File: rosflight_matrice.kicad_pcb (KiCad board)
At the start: 2 copper layers, 80 x 49 mm, 21 parts, among them J1 Left, J10 I2C, J11 I2C, J2 Right, J3 Power, J4 Servo 1-3, J5 Servo 4-6, J6 Main, J7 Flexi-IO, J8 Flexi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

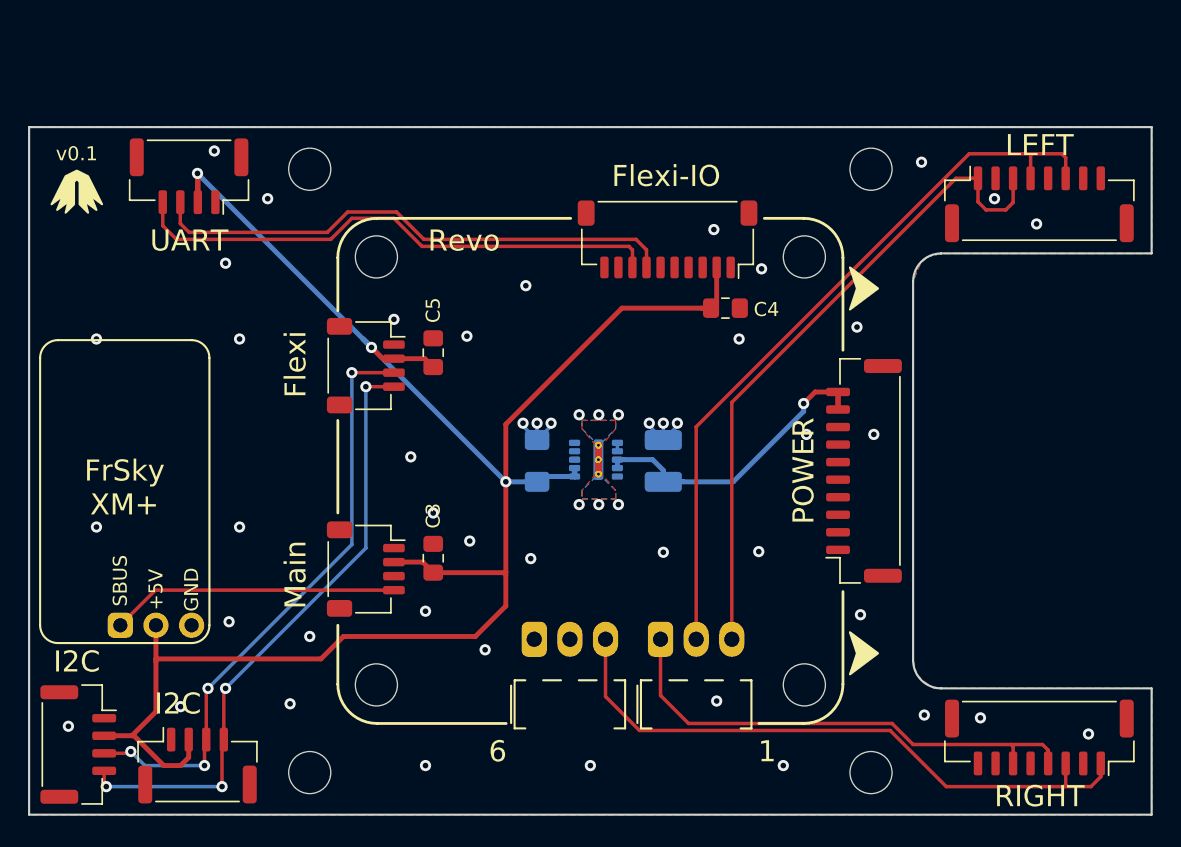
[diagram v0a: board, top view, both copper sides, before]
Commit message: New switching voltage regulator and updated layout
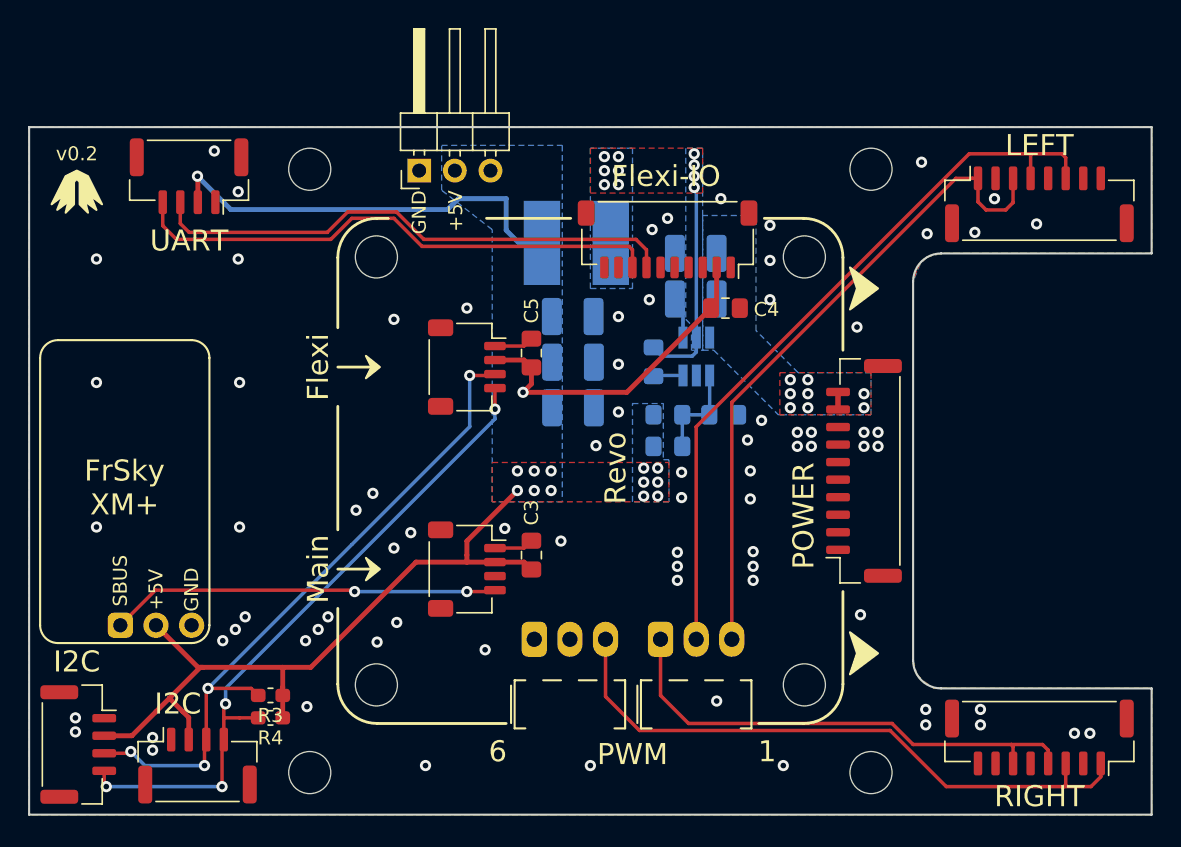
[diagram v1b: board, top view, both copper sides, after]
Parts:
- added C10: 22uF, Capacitor_SMD:C_1210_3225Metric_Pad1.42x2.65mm_HandSolder, B.Cu at (148.8, 95.5)
- added C6: 100nF, Capacitor_SMD:C_0805_2012Metric_Pad1.15x1.40mm_HandSolder, B.Cu at (154.5, 92.2)
- added C7: 100pF, Capacitor_SMD:C_0805_2012Metric_Pad1.15x1.40mm_HandSolder, B.Cu at (155.5, 98.2)
- added C8: 22uF, Capacitor_SMD:C_1210_3225Metric_Pad1.42x2.65mm_HandSolder, B.Cu at (148.7, 89.0)
- added C9: 22uF, Capacitor_SMD:C_1210_3225Metric_Pad1.42x2.65mm_HandSolder, B.Cu at (148.8, 92.2)
- added J12: 5V, Connector_PinHeader_2.54mm:PinHeader_1x03_P2.54mm_Horizontal, F.Cu at (137.8, 78.6)
- added L1: 6.8uH, quadrotor:SRN6045_HandSolder, B.Cu at (149.0, 83.8)
- added R1: 100k, Resistor_SMD:R_0805_2012Metric_Pad1.15x1.40mm_HandSolder, B.Cu at (155.5, 96.0)
- added R2: 13.7k, Resistor_SMD:R_0805_2012Metric_Pad1.15x1.40mm_HandSolder, B.Cu at (159.5, 96.0)
- added R3: 4.7k, Resistor_SMD:R_0603_1608Metric_Pad1.05x0.95mm_HandSolder, F.Cu at (127.2, 116.0)
- added R4: 4.7k, Resistor_SMD:R_0603_1608Metric_Pad1.05x0.95mm_HandSolder, F.Cu at (127.2, 117.6)
- C2: value 22uF -> 10uF; footprint Capacitor_SMD:C_1206_3216Metric_Pad1.42x1.75mm_HandSolder -> Capacitor_SMD:C_1210_3225Metric_Pad1.42x2.65mm_HandSolder
- U1: value LMZM23600V5SIL -> TPS54202; footprint Package_LGA:Texas_SIL0010A_MicroSiP-10-1EP_3.8x3mm_P0.6mm_EP0.7x2.9mm_ThermalVias -> Package_TO_SOT_SMD:SOT-23-6_Handsoldering
- moved C2 16.2 mm to (157.5, 87.8), turned to 180 degrees
- moved C1 15.0 mm to (157.5, 84.5), turned to 180 degrees
- moved U1 10.3 mm to (157.6, 91.8), turned to 270 degrees
- moved J8 7.20 mm to (141.2, 92.6)
- moved J6 7.20 mm to (141.2, 107.0)
- moved C3 7.00 mm to (145.8, 106.0)
- moved C5 7.00 mm to (145.8, 91.6)
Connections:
- C2 pad 1: +5V -> +BATT
- U1 pad 2: GND -> Net-(C6-Pad1)
- U1 pad 4: +BATT -> Net-(C7-Pad2)
- U1 pad 6: +5V -> Net-(C6-Pad2)
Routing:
- net +5V: track 129.6 -> 108.2 mm, vias 3 -> 14
- net +BATT: track 21.7 -> 1.25 mm, vias 1 -> 8
- net Net-(C6-Pad1): track 0.00 -> 15.2 mm, vias 0 -> 10
- net /SBUS: track 20.5 -> 27.8 mm, vias 0 -> 2
- net Net-(C7-Pad2): track 0.00 -> 6.99 mm
- net /SCL: track 43.0 -> 48.9 mm
- net /SDA: track 44.2 -> 48.3 mm
- net Net-(C6-Pad2): track 0.00 -> 2.12 mm
- net GND: track 9.46 -> 8.62 mm, vias 52 -> 78
- added copper zone on B.Cu, net +5V
- added copper zone on F.Cu, net +5V
- added copper zone on B.Cu, net +BATT
- added copper zone on F.Cu, net +BATT
- added copper zone on B.Cu, net Net-(C6-Pad1)
- added copper zone on F.Cu, net Net-(C6-Pad1)
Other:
- board text added: "+5V"
- board text added: "GND"
- board text added: "PWM"
- board text added: "v0.2"
- board text removed: "v0.1"
